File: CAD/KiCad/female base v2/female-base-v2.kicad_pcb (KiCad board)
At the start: 2 copper layers, 50 x 80 mm, 14 parts, among them J2 dxl mirror, J3 microphone, J4 photosensor, J5 neopixel, J6 Speaker, J7 DA15_Plug_MountingHoles, M1 GF1002 direct module

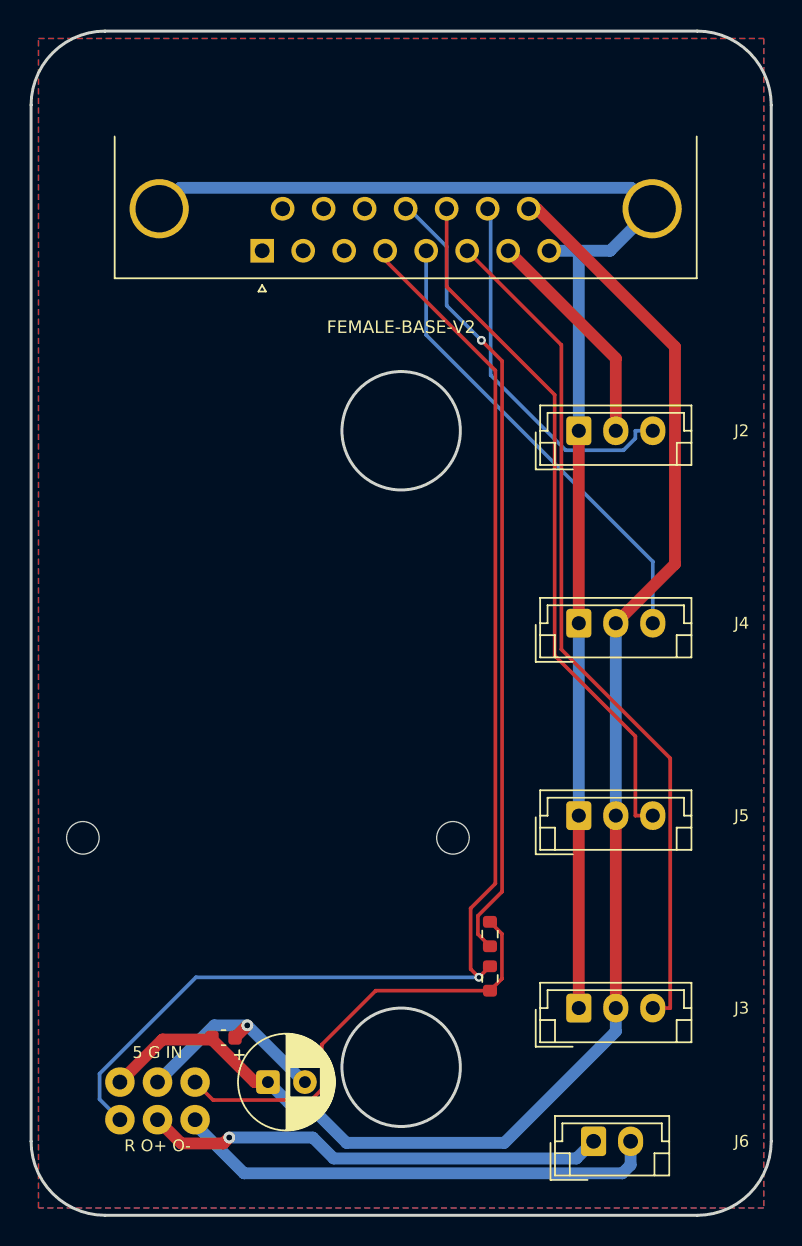
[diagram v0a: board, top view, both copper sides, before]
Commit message: Keep the GF1002 contact row clear on both body boards
Correct the reference to nine contacts on the long edge. Move H2 to the short end, move hookup pads alongside the row, clear nearby components and require flush-cut pin tails. Preserve artwork outlines, DSUB geometry and harness pin order.

Refresh routed PCBs, STEP/VRML models, body scenes, production Gerbers and actual-size templates. User approved the documented dimensional estimates; physical fit and ROUT polarity remain checks before ordering. Native ERC/DRC/parity and clearance checks pass; all 1796 pytest tests pass.
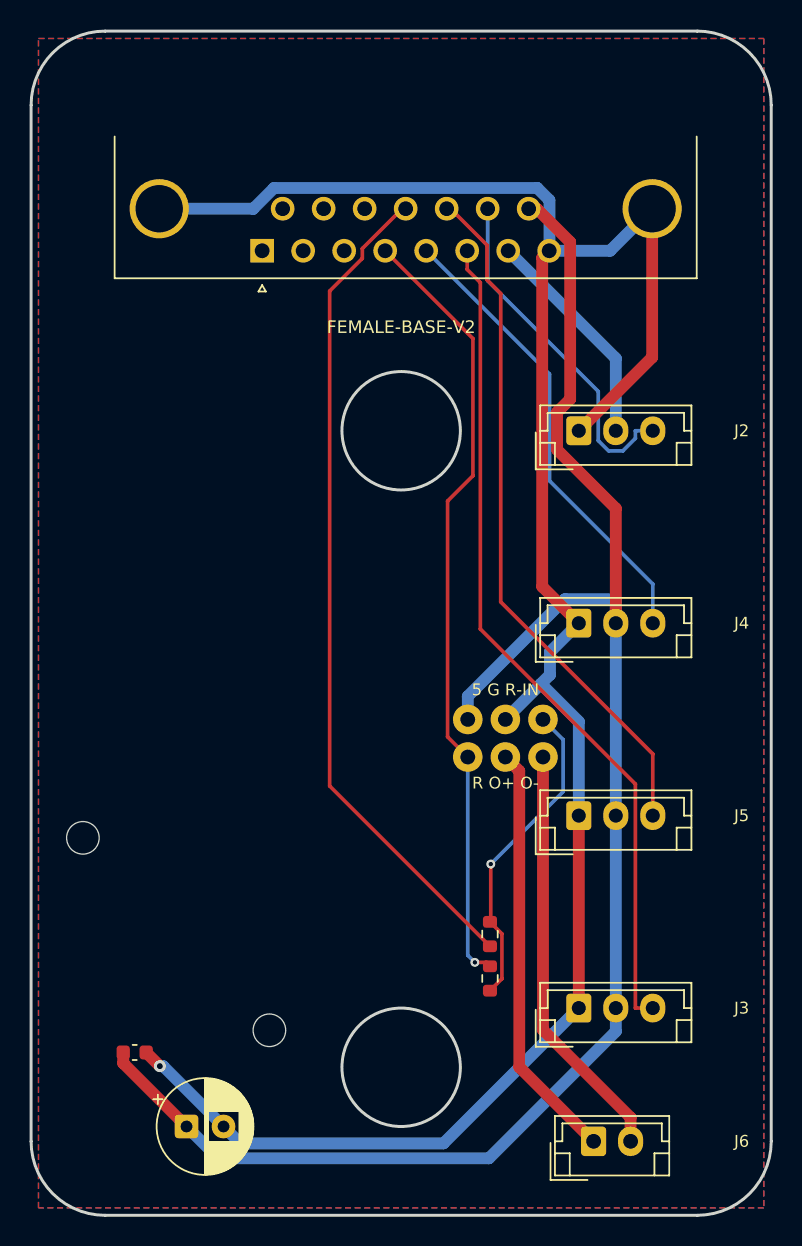
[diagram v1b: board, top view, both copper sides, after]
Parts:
- H2: footprint Body:GF1002_Clamp_Right -> Body:GF1002_Clamp_End
- moved JA1 33.9 mm to (54.5, 66.5)
- moved H2 18.0 mm to (41.1, 87.5), turned to 90 degrees
- moved C1 6.26 mm to (35.5, 94.0)
- moved C2 6.08 mm to (32.0, 89.0)
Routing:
- net GND: track 108.1 -> 149.3 mm
- net AUDIO_RETURN: track 86.1 -> 53.1 mm
- net 5V: track 102.5 -> 115.1 mm
- net AMP_INPUT: track 30.6 -> 21.6 mm, vias 0 -> 1
- net AMP_OUT_N: track 32.9 -> 28.4 mm
- net AMP_OUT_P: track 31.4 -> 28.4 mm, vias 1 -> 0
- net LINE_IN: track 53.7 -> 56.6 mm, vias 1 -> 0
- net dynamixel data: track 25.2 -> 23.6 mm
- net microphone output: track 58.0 -> 57.0 mm
- net neopixel input: track 47.5 -> 46.9 mm
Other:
- board text added: "5 G R-IN"
- board text added: "TRIM MODULE PINS FLUSH / VERIFY FIT"
- board text removed: "5 G IN"

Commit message: Socket and reroute the body amplifiers to revision D
Replace JA1 wires with eleven-pin GF1002 sockets, explicit unused contacts and an 11 mm header stack. Move the divider and bypass beside their socket pins, shorten and pair the speaker routes, and separate them from audio and sensor inputs with a grounded guard. Add adjustable support models and preserve the artwork outline, DSUB geometry and harness pin order.

Regenerate schematics, routing, models, current body scenes, Gerbers and actual-size templates. Native ERC/DRC/unconnected/parity are zero on both boards; independent socket, support, decoupling and routing checks pass; all 1796 pytest tests pass. Module fit, purchased stack height, module ground bond and ROUT polarity remain physical checks before ordering.
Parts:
- removed JA1: GF1002 wire connections, Body:GF1002_WirePads_2x03
- H1: value M2 insulating clamp -> M2 insulating support / 11mm; footprint Body:GF1002_Clamp_Left -> Body:GF1002_Support_Left
- H2: value M2 insulating clamp -> M2 insulating support / 11mm; footprint Body:GF1002_Clamp_End -> Body:GF1002_Support_End
- M1: value GF1002 direct module -> GF1002 / 1x11 female socket; footprint Body:GF1002_Module_Direct -> Body:GF1002_PlugIn_1x11
- moved C1 34.0 mm to (55.5, 66.5)
- moved J3 29.1 mm to (34.0, 94.0)
- moved R1 27.6 mm to (44.0, 56.2), turned to 0 degrees
- moved R2 27.2 mm to (45.8, 58.7), turned to 0 degrees
- moved C2 25.4 mm to (45.7, 67.6)
- moved M1 18.6 mm to (49.5, 56.2)
- moved J6 7.07 mm to (64.0, 88.0), turned to -90 degrees
- moved J4 2.69 mm to (63.0, 57.5)
- moved J5 1.80 mm to (63.0, 74.5)
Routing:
- net LINE_IN: track 56.6 -> 28.0 mm, vias 0 -> 1
- net 5V: track 115.1 -> 97.5 mm
- net AUDIO_RETURN: track 53.1 -> 36.9 mm
- net AMP_INPUT: track 21.6 -> 7.26 mm, vias 1 -> 0
- net AMP_OUT_P: track 28.4 -> 18.2 mm
- net microphone output: track 57.0 -> 67.1 mm
- net AMP_OUT_N: track 28.4 -> 19.2 mm
- net dynamixel data: track 23.6 -> 19.7 mm, vias 0 -> 1
- net GND: track 149.3 -> 152.0 mm, vias 1 -> 0
- net neopixel input: track 46.9 -> 49.5 mm
- net photo sensor output: track 31.5 -> 30.3 mm
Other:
- board text added: "FIT HEADERS / VERIFY STACK AND POLARITY"
- board text added: "GF1002 / PLUG-IN / 11mm STACK"
- board text added: "R IN"
- board text added: "ROUT +/- VERIFY"
- board text removed: "5 G R-IN"
- board text removed: "GF1002 / DIRECT / NO PERFBOARD"
- board text removed: "R O+ O-"
- board text removed: "TRIM MODULE PINS FLUSH / VERIFY FIT"

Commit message: Use SMD reservoir capacitors on both v2 body boards
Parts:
- C1: footprint Capacitor_THT:CP_Radial_D6.3mm_P2.50mm -> Capacitor_SMD:CP_Elec_6.3x5.8
- moved C1 3.60 mm to (59.1, 66.5)
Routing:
- net 5V: track 97.5 -> 101.3 mm, vias 0 -> 1
- net GND: track 152.0 -> 150.1 mm

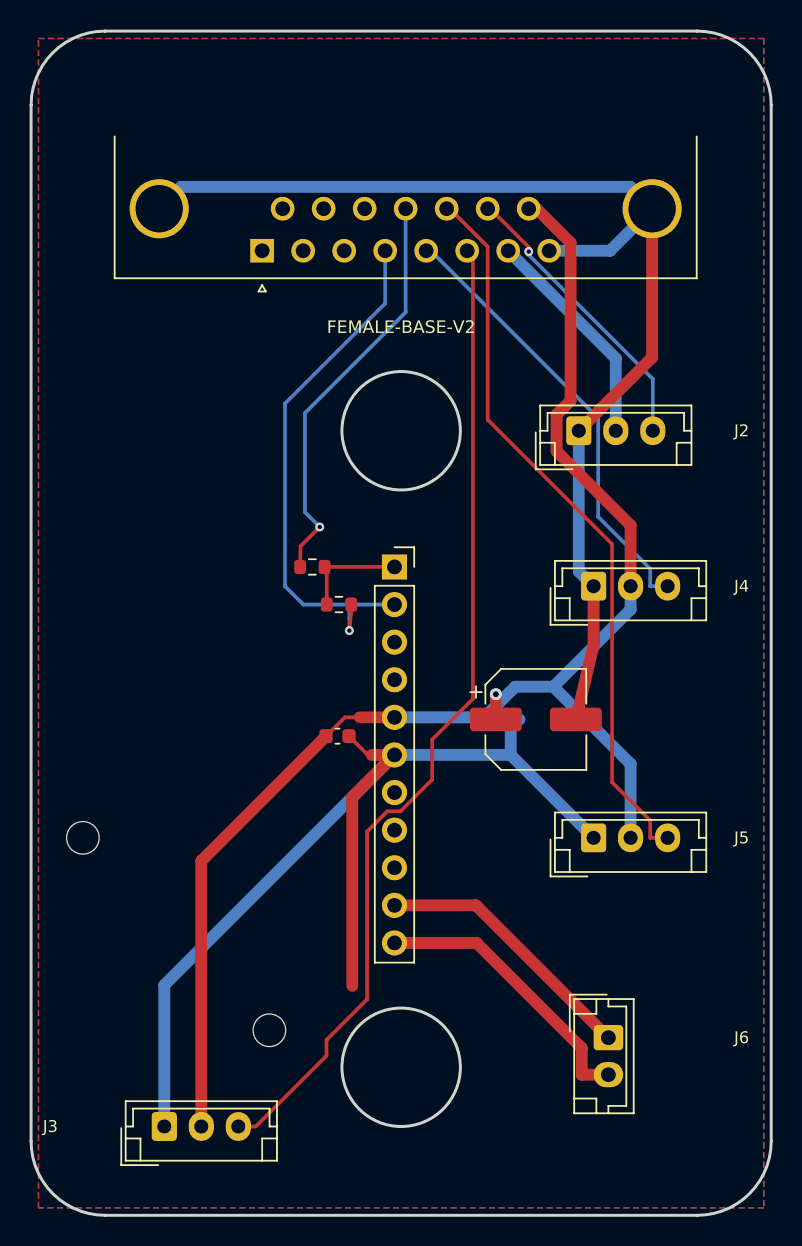
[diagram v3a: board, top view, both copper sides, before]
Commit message: Name every body-board connector on the front silkscreen
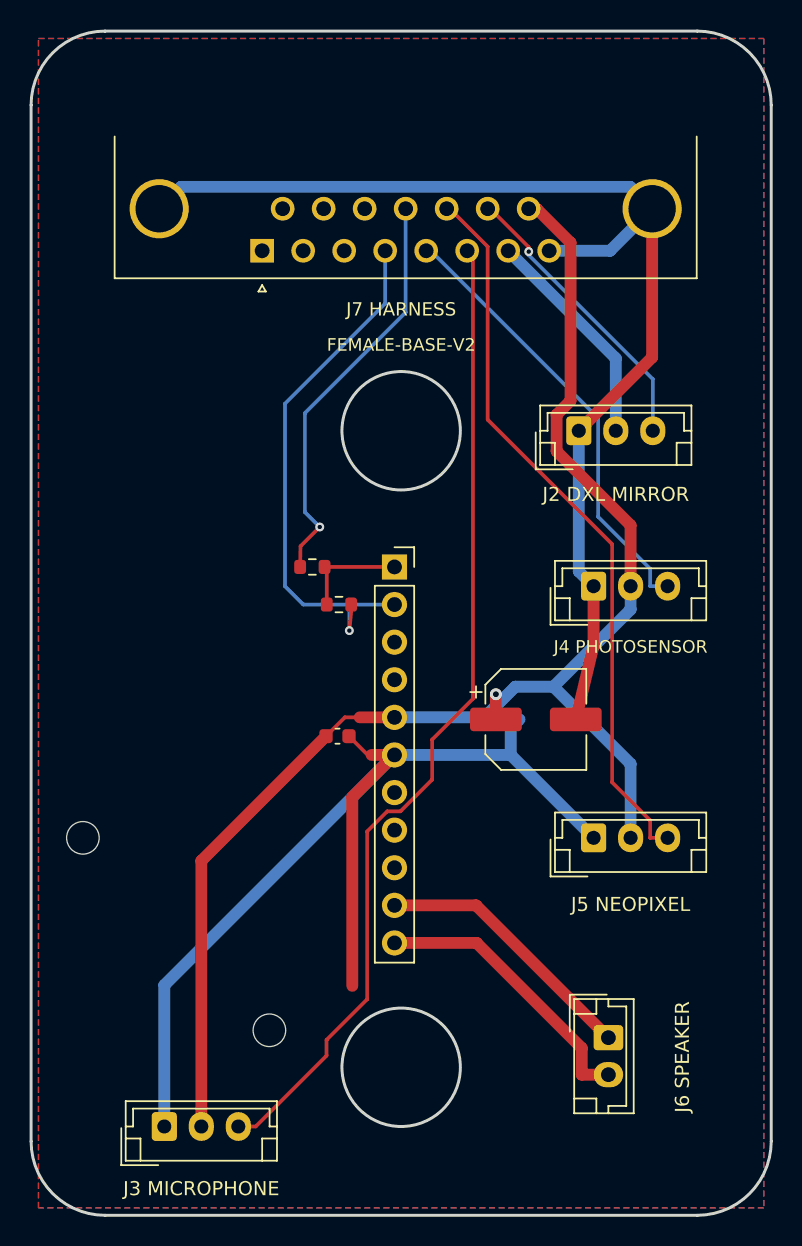
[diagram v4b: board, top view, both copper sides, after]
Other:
- board text added: "J2 DXL MIRROR"
- board text added: "J3 MICROPHONE"
- board text added: "J4 PHOTOSENSOR"
- board text added: "J5 NEOPIXEL"
- board text added: "J6 SPEAKER"
- board text added: "J7 HARNESS"
- board text removed: "J2"
- board text removed: "J3"
- board text removed: "J4"
- board text removed: "J5"
- board text removed: "J6"
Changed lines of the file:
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@@
 	)
 	(gr_text "FEMALE-BASE-V2"
-		(at 50 40 0)
+		(at 50 41.2 0)
 		(layer "F.SilkS")
 		(effects
@@
 		)
 	)
-	(gr_text "J5"
-		(at 73 74.5 0)
+	(gr_text "J7 HARNESS"
+		(at 50 38.8 0)
 		(layer "F.SilkS")
 		(effects
 			(font
-				(size 0.8 0.8)
-				(thickness 0.12)
+				(size 0.9 0.9)
+				(thickness 0.15)
 			)
 		)
 	)
-	(gr_text "J2"
-		(at 73 47 0)
+	(gr_text "J6 SPEAKER"
+		(at 69 89.3 90)
 		(layer "F.SilkS")
 		(effects
 			(font
-				(size 0.8 0.8)
-				(thickness 0.12)
+				(size 0.95 0.95)
+				(thickness 0.15)
 			)
 		)
 	)
-	(gr_text "J4"
-		(at 73 57.5 0)
+	(gr_text "J5 NEOPIXEL"
+		(at 65.5 79 0)
 		(layer "F.SilkS")
 		(effects
 			(font
-				(size 0.8 0.8)
-				(thickness 0.12)
+				(size 0.95 0.95)
+				(thickness 0.15)
 			)
 		)
 	)
-	(gr_text "J3"
-		(at 26.3 94 0)
+	(gr_text "J4 PHOTOSENSOR"
+		(at 65.5 61.6 0)
 		(layer "F.SilkS")
 		(effects
 			(font
-				(size 0.8 0.8)
-				(thickness 0.12)
+				(size 0.85 0.85)
+				(thickness 0.15)
 			)
 		)
 	)
-	(gr_text "J6"
-		(at 73 88 0)
+	(gr_text "J3 MICROPHONE"
+		(at 36.5 98.2 0)
 		(layer "F.SilkS")
 		(effects
 			(font
-				(size 0.8 0.8)
-				(thickness 0.12)
+				(size 0.95 0.95)
+				(thickness 0.15)
 			)
 		)
+	)
+	(gr_text "J2 DXL MIRROR"
+		(at 64.5 51.3 0)
+		(layer "F.SilkS")
+		(effects
+			(font
+				(size 0.95 0.95)
+				(thickness 0.15)
+			)
+		)

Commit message: Reroute the female base around the revised placement and removed support holes
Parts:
- removed H1: M2 insulating support / 11mm, Body:GF1002_Support_Left
- removed H2: M2 insulating support / 11mm, Body:GF1002_Support_End
- moved C1 31.9 mm to (33.9, 47.0), turned to 180 degrees
- moved C2 11.6 mm to (34.1, 67.6), turned to 180 degrees
- moved R1 4.61 mm to (39.5, 57.4)
- moved R2 4.61 mm to (41.3, 59.9)
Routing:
- net 5V: track 101.3 -> 141.1 mm, vias 1 -> 0
- net GND: track 150.1 -> 181.5 mm
- net AUDIO_RETURN: track 36.9 -> 47.0 mm
- net AMP_INPUT: track 7.26 -> 12.3 mm
- net LINE_IN: track 28.0 -> 32.6 mm
- net 12V: track 15.2 -> 19.1 mm
- net photo sensor output: track 30.3 -> 33.3 mm
- net dynamixel data: track 19.7 -> 20.3 mm, vias 1 -> 0
- net neopixel input: track 49.5 -> 49.4 mm, vias 0 -> 1
